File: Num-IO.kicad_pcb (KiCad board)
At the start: 4 copper layers, 170.2 x 77.5 mm, 143 parts, among them J1 DB37_Female, J2 DB37_Male, J3 Conn_02x25_Odd_Even, J4 0826-1X1T-GH-F, U1 MAX14917AFM+, U10 LTC6820IUD, U11 LTC6820IUD, U12 LTC6820IUD, U13 LTC6820IUD, U2 MAX14917AFM+, U3 74LVC1G18, U4 MAX14851AEE+, U5 MAX14917AFM+, U6 MAX31910AUI+, U7 MAX31910AUI+, U8 MAX31910AUI+, U9 MAX31910AUI+

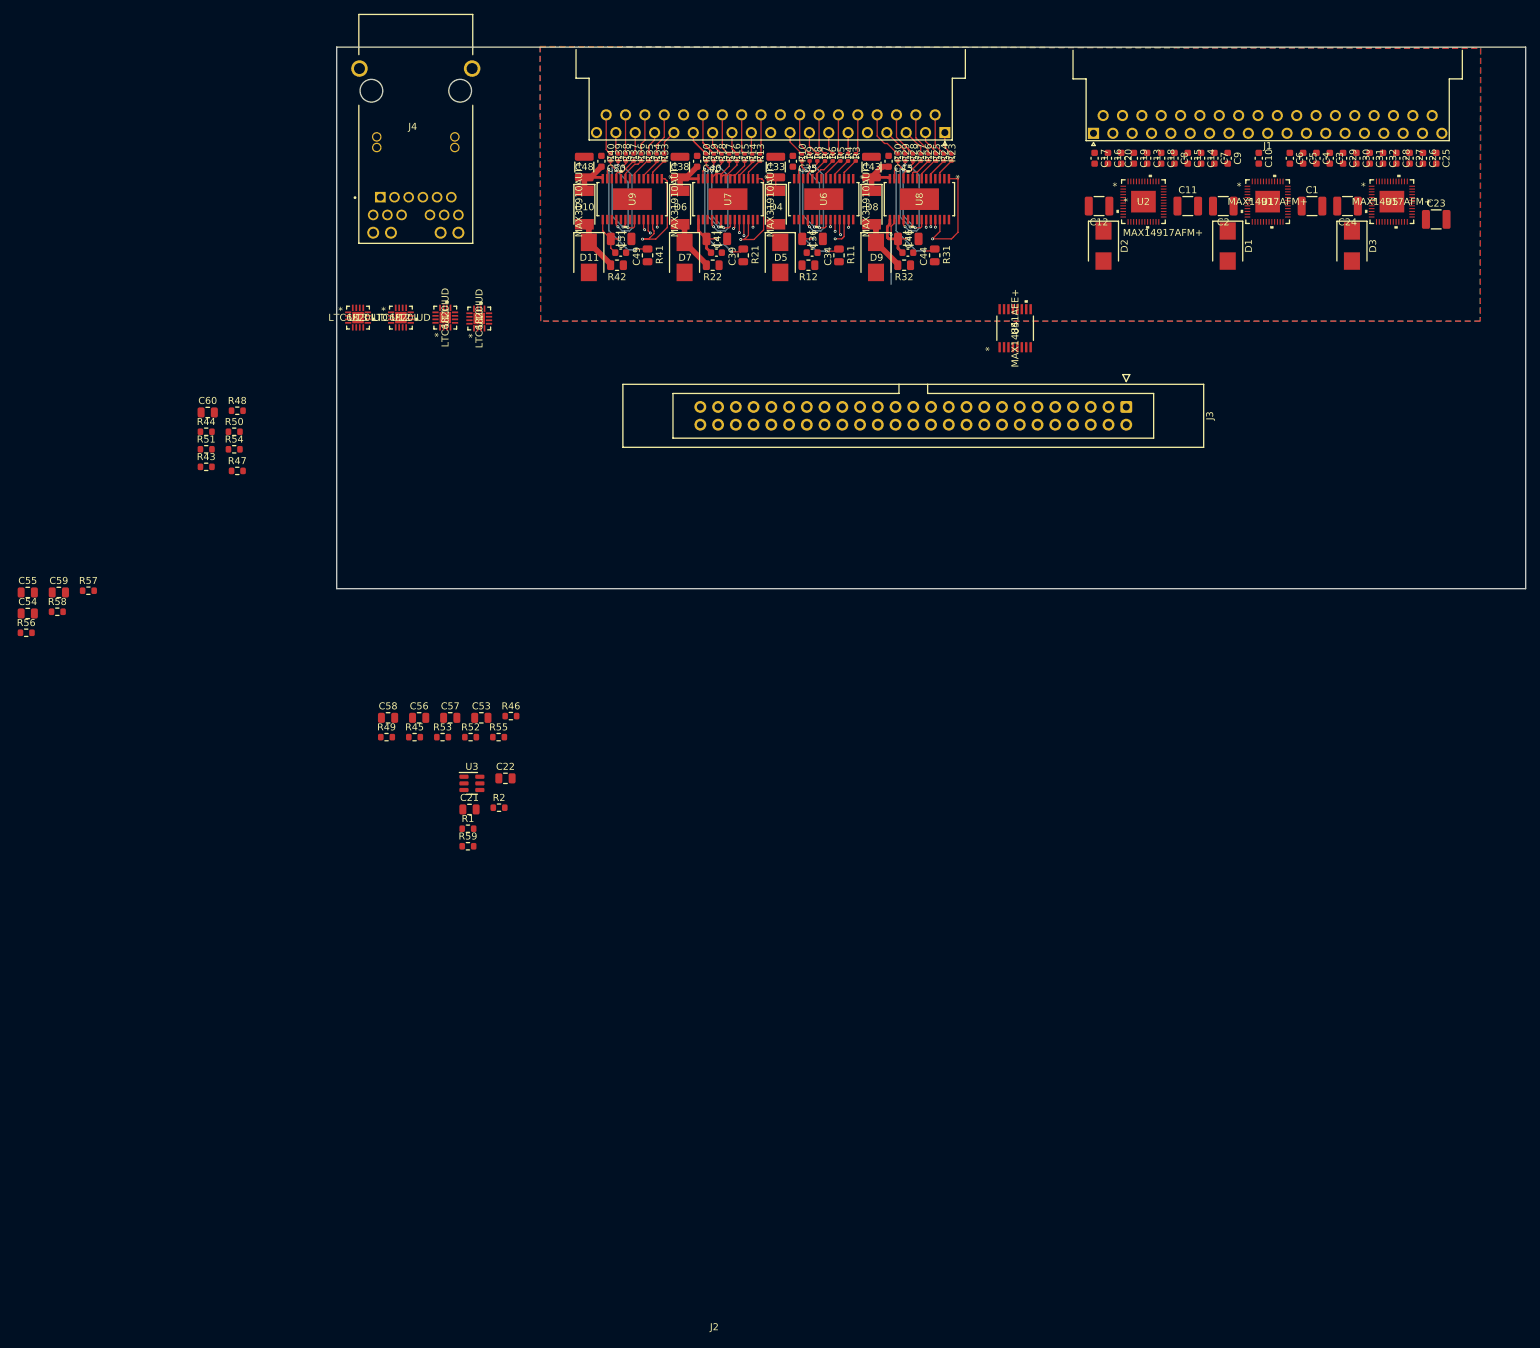
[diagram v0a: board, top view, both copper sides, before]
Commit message: Common power stage for field IO
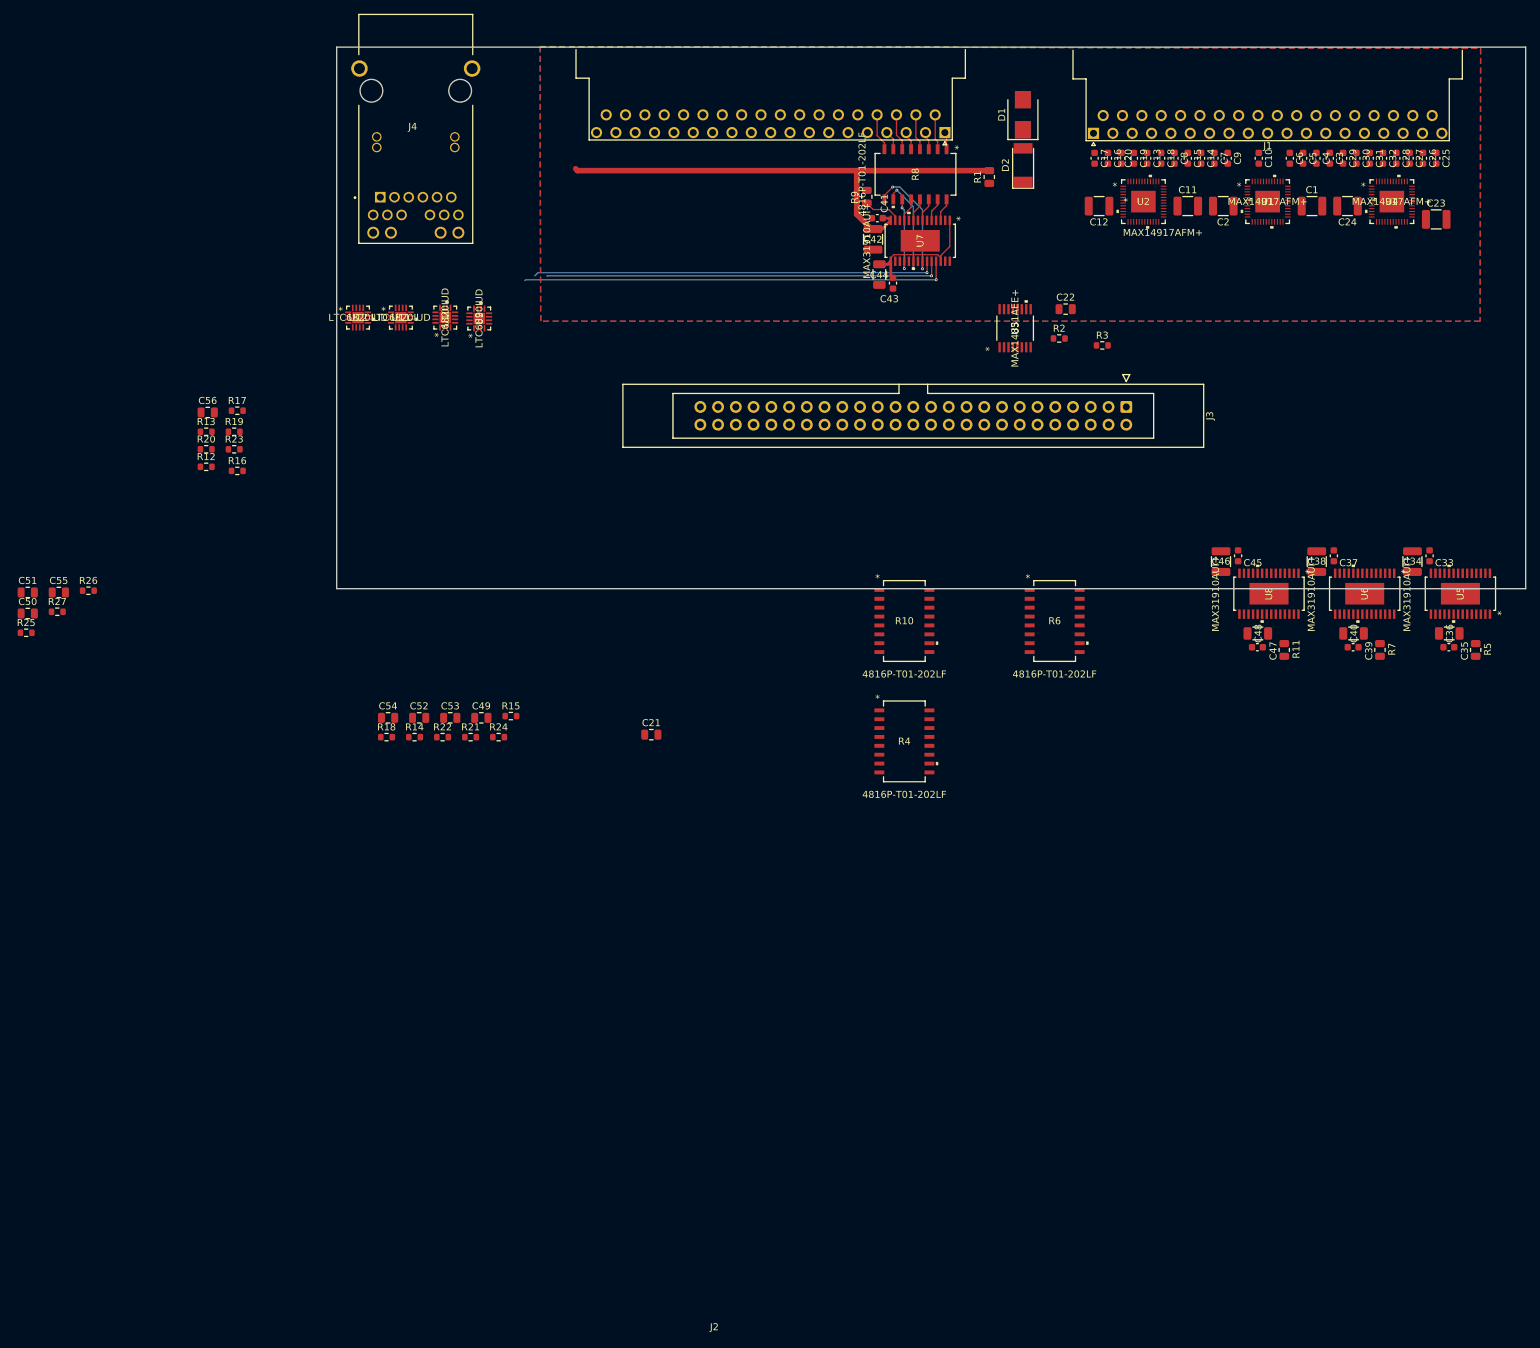
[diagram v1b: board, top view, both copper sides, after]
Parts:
- removed D10, D4, D6, D8: 1N4007, Diode_SMD:D_MELF
- removed D11, D5, D7, D9: SM6T36A, Diode_SMD:D_SMB
- removed D3: SM6F36A, Diode_SMD:D_SMB
- removed the R12 at (127.3, 55.5)
- removed the R13 at (120.4, 40.0)
- removed the R14 at (119.3, 40.0)
- removed the R15 at (118.2, 40.0)
- removed the R16 at (117.1, 40.0)
- removed the R17 at (116.0, 40.0)
- removed the R18 at (114.9, 40.0)
- removed the R19 at (113.8, 40.0)
- removed the R20 at (112.7, 40.0)
- removed the R22 at (113.6, 55.5)
- removed the R23 at (147.8, 40.0)
- removed the R24 at (146.7, 40.0)
- removed the R25 at (145.6, 40.0)
- removed the R26 at (144.5, 40.0)
- removed the R27 at (143.4, 40.0)
- removed R28, R29, R30, R33, R34, R35, R36, R37, R38, R39, R40: 2.2k, Resistor_SMD:R_0402_1005Metric
- removed the R3 at (134.1, 40.0)
- removed R32, R42: 150R, Resistor_SMD:R_0805_2012Metric
- removed the R5 at (131.9, 40.0)
- removed the R7 at (129.7, 40.0)
- removed the R9 at (127.5, 40.0)
- removed the U3 at (79.2, 129.6)
- D1: value SM6F36A -> SM6T36A
- D2: value SM6F36A -> 1N4007; footprint Diode_SMD:D_SMB -> Diode_SMD:D_MELF
- R1: value 3.3k -> 150R; footprint Resistor_SMD:R_0603_1608Metric -> Resistor_SMD:R_0805_2012Metric
- R10, R4, R6, R8: value 2.2k -> 4816P-T01-202LF; footprint Resistor_SMD:R_0402_1005Metric -> Maxim industrial IO:4816P
- moved R1 119.4 mm to (153.2, 42.8), turned to 90 degrees
- moved R3 115.7 mm to (169.4, 66.9)
- moved C34 107.2 mm to (213.8, 97.9)
- moved C37 107.2 mm to (202.5, 97.0)
- moved C47 107.2 mm to (191.6, 110.1)
- moved C33 107.2 mm to (216.2, 97.0)
- moved C35 107.2 mm to (219.0, 110.1)
- moved C36 107.2 mm to (219.0, 108.2)
- moved C38 107.2 mm to (200.1, 97.9)
- moved C39 107.2 mm to (205.3, 110.1)
- moved C40 107.2 mm to (205.3, 108.2)
- moved C45 107.2 mm to (188.8, 97.0)
- moved C46 107.2 mm to (186.4, 97.9)
- moved C48 107.2 mm to (191.6, 108.2)
- moved R11 107.2 mm to (195.4, 110.5)
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- renumbered C35 to C33, C33 to C34, C34 to C35, C40 to C37, C41 to C40, C45 to C41, C43 to C42, C44 to C43, C46 to C44, C50 to C45, C48 to C46, C49 to C47, C51 to C48, C53 to C49, C54 to C50, C55 to C51, C56 to C52, C57 to C53, C58 to C54, C59 to C55, C60 to C56, R41 to R11, R43 to R12, R44 to R13, R45 to R14, R46 to R15, R47 to R16, R48 to R17, R49 to R18, R50 to R19, R51 to R20, R52 to R21, R53 to R22, R54 to R23, R55 to R24, R56 to R25, R57 to R26, R58 to R27, R59 to R3, R11 to R5, R21 to R7, R31 to R9, U11 to U10, U12 to U11, U13 to U12, U4 to U3, U5 to U4, U6 to U5, U7 to U6, U8 to U7, U9 to U8, U10 to U9
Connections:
- net GND renamed GNDD
- C12 pad 1: +24V -> OUTPWR
- C2 pad 1: +24V -> OUTPWR
- C24 pad 1: +24V -> OUTPWR
- C33 pad 1: Net-(C33-Pad1) -> INPWR
- C34 pad 1: Net-(C33-Pad1) -> INPWR
- C37 pad 1: Net-(C38-Pad1) -> INPWR
- C38 pad 1: Net-(C38-Pad1) -> INPWR
- C41 pad 1: Net-(C43-Pad1) -> INPWR
- C42 pad 1: Net-(C43-Pad1) -> INPWR
- C45 pad 1: Net-(C48-Pad1) -> INPWR
- C46 pad 1: Net-(C48-Pad1) -> INPWR
- D2 pad 1: +24V -> OUTPWR
- D2 pad 2: GNDPWR -> +24V
- R1 pad 1: /CS0 -> OUTPWR
- R1 pad 2: /IsoPWR -> INPWR
- R10 pad 1: /Input connector/IN16 -> /Input connector/IN25
- R10 pad 2: Net-(R10-Pad2) -> /Input connector/IN26
- R2 pad 1: /CS1 -> /CS
- R4 pad 1: /Input connector/IN10 -> /Input connector/IN9
- R4 pad 2: Net-(R4-Pad2) -> /Input connector/IN10
- R6 pad 1: /Input connector/IN12 -> /Input connector/IN17
- R6 pad 2: Net-(R6-Pad2) -> /Input connector/IN18
- R8 pad 1: /Input connector/IN14 -> /Input connector/IN1
- R8 pad 2: Net-(R8-Pad2) -> /Input connector/IN2
- U1 pad 30: /CS1 -> /CS
- U1 pad 49: +24V -> OUTPWR
- U1 pad 8: +24V -> OUTPWR
- U2 pad 30: /CS1 -> /CS
- U2 pad 34: /SDO -> GNDPWR
- U2 pad 49: +24V -> OUTPWR
- U2 pad 8: +24V -> OUTPWR
- U3 pad 10: /CS0 -> unconnected-(U3-Pad10)
- U3 pad 11: /CS1 -> /CS
- U3 pad 6: Net-(U3-Pad6) -> /FPGA Connector/SPI0.*CS
- U3 pad 7: Net-(U3-Pad4) -> unconnected-(U3-Pad7)
- U4 pad 30: /CS1 -> /CS
- U4 pad 49: +24V -> OUTPWR
- U4 pad 8: +24V -> OUTPWR
- U5 pad 11: Net-(R7-Pad2) (its old number) -> Net-(R4-Pad12)
- U5 pad 14: Net-(C33-Pad1) -> INPWR
- U5 pad 18: Net-(R8-Pad2) -> Net-(R4-Pad11)
- U5 pad 20: Net-(R9-Pad2) (its old number) -> Net-(R4-Pad10)
- U5 pad 22: Net-(R10-Pad2) -> Net-(R4-Pad9)
- U5 pad 24: /CS0 -> /CS
- U5 pad 3: Net-(R3-Pad2) -> Net-(R4-Pad16)
- U5 pad 5: Net-(R4-Pad2) -> Net-(R4-Pad15)
- U5 pad 7: Net-(R5-Pad2) (its old number) -> Net-(R4-Pad14)
- U5 pad 9: Net-(R6-Pad2) -> Net-(R4-Pad13)
- U6 pad 11: Net-(R17-Pad2) (its old number) -> Net-(R6-Pad12)
- U6 pad 14: Net-(C38-Pad1) -> INPWR
- U6 pad 18: Net-(R18-Pad2) (its old number) -> Net-(R6-Pad11)
- U6 pad 20: Net-(R19-Pad2) (its old number) -> Net-(R6-Pad10)
- U6 pad 22: Net-(R20-Pad2) -> Net-(R6-Pad9)
- U6 pad 24: /CS0 -> /CS
- U6 pad 3: Net-(R13-Pad2) -> Net-(R6-Pad16)
- U6 pad 5: Net-(R14-Pad2) -> Net-(R6-Pad15)
- U6 pad 7: Net-(R15-Pad2) -> Net-(R6-Pad14)
- U6 pad 9: Net-(R16-Pad2) (its old number) -> Net-(R6-Pad13)
- U7 pad 11: Net-(R27-Pad2) -> Net-(R8-Pad12)
- U7 pad 14: Net-(C43-Pad1) -> INPWR
- U7 pad 18: Net-(R28-Pad2) -> Net-(R8-Pad11)
- U7 pad 20: Net-(R29-Pad2) -> Net-(R8-Pad10)
- U7 pad 22: Net-(R30-Pad2) -> Net-(R8-Pad9)
- U7 pad 24: /CS0 -> /CS
- U7 pad 3: Net-(R23-Pad2) -> Net-(R8-Pad16)
- U7 pad 5: Net-(R24-Pad2) -> Net-(R8-Pad15)
- U7 pad 7: Net-(R25-Pad2) -> Net-(R8-Pad14)
- U7 pad 9: Net-(R26-Pad2) -> Net-(R8-Pad13)
- U8 pad 11: Net-(R37-Pad2) -> Net-(R10-Pad12)
- U8 pad 14: Net-(C48-Pad1) -> INPWR
- U8 pad 18: Net-(R38-Pad2) -> Net-(R10-Pad11)
- U8 pad 20: Net-(R39-Pad2) -> Net-(R10-Pad10)
- U8 pad 22: Net-(R40-Pad2) -> Net-(R10-Pad9)
- U8 pad 24: /CS0 -> /CS
- U8 pad 3: Net-(R33-Pad2) -> Net-(R10-Pad16)
- U8 pad 5: Net-(R34-Pad2) -> Net-(R10-Pad15)
- U8 pad 7: Net-(R35-Pad2) -> Net-(R10-Pad14)
- U8 pad 9: Net-(R36-Pad2) -> Net-(R10-Pad13)
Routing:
- net INPWR: track 0.00 -> 73.1 mm
- net /CS: track 0.00 -> 57.1 mm, vias 0 -> 1
- net /CS0: track 48.1 -> 0.00 mm, vias 4 -> 0
- net /input channel 1-8/SDO: track 13.8 -> 58.0 mm, vias 2 -> 1
- net /IsoPWR: track 26.1 -> 0.00 mm, vias 2 -> 0
- net /input channel 17-24/5VOUT: track 25.9 -> 0.00 mm, vias 2 -> 0
- net Net-(R7-Pad2): track 17.6 -> 0.00 mm, vias 2 -> 0
- net Net-(R8-Pad9): track 0.00 -> 17.4 mm, vias 0 -> 2
- net Net-(R5-Pad2): track 17.3 -> 0.00 mm, vias 2 -> 0
- net Net-(R11-Pad2): track 17.0 -> 0.00 mm, vias 2 -> 0
- net Net-(R8-Pad10): track 0.00 -> 14.8 mm, vias 0 -> 2
- net Net-(R18-Pad2) (its old number): track 13.9 -> 0.00 mm, vias 2 -> 0
- net Net-(R38-Pad2): track 13.9 -> 0.00 mm, vias 2 -> 0
- net Net-(R8-Pad2): track 13.9 -> 0.00 mm, vias 2 -> 0
- net Net-(R28-Pad2): track 13.9 -> 0.00 mm, vias 2 -> 0
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
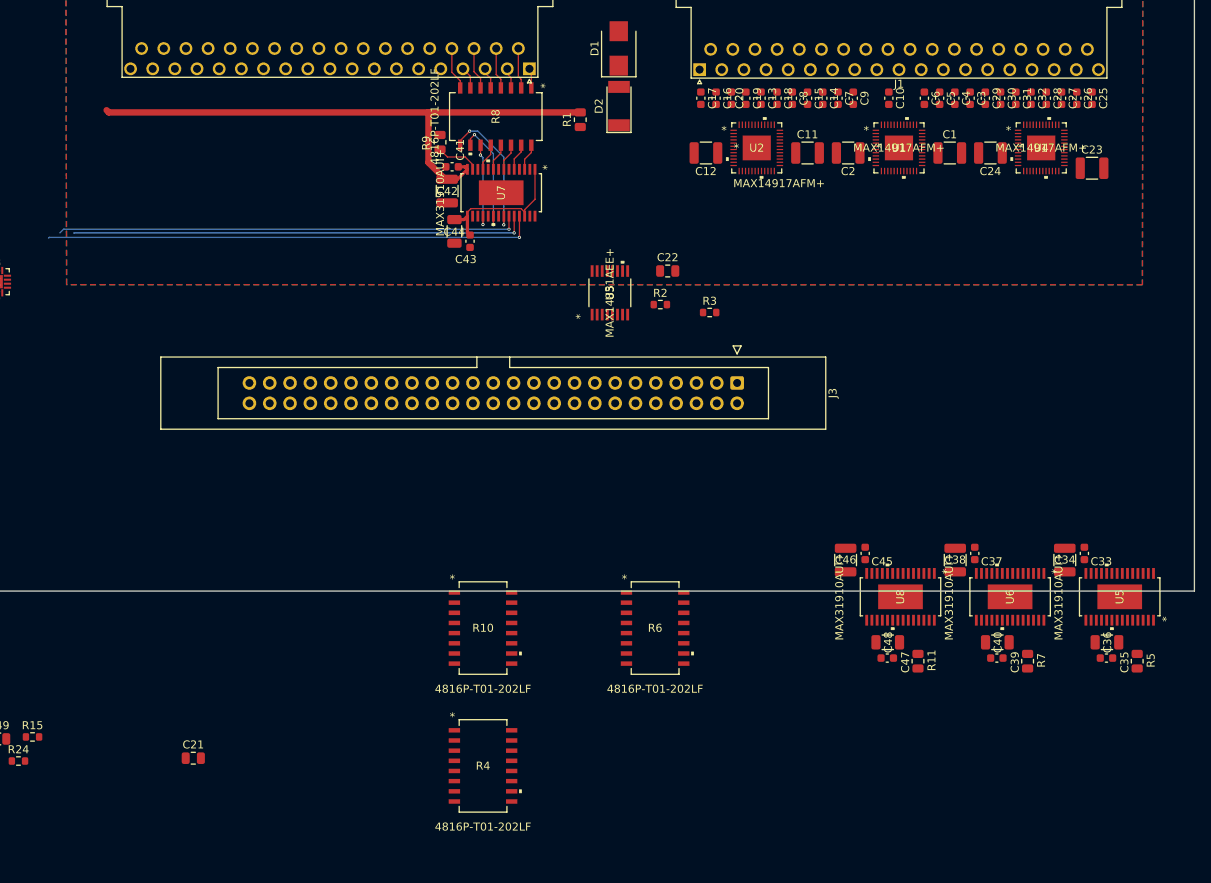
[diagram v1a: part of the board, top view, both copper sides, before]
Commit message: Further simplifying the schematics
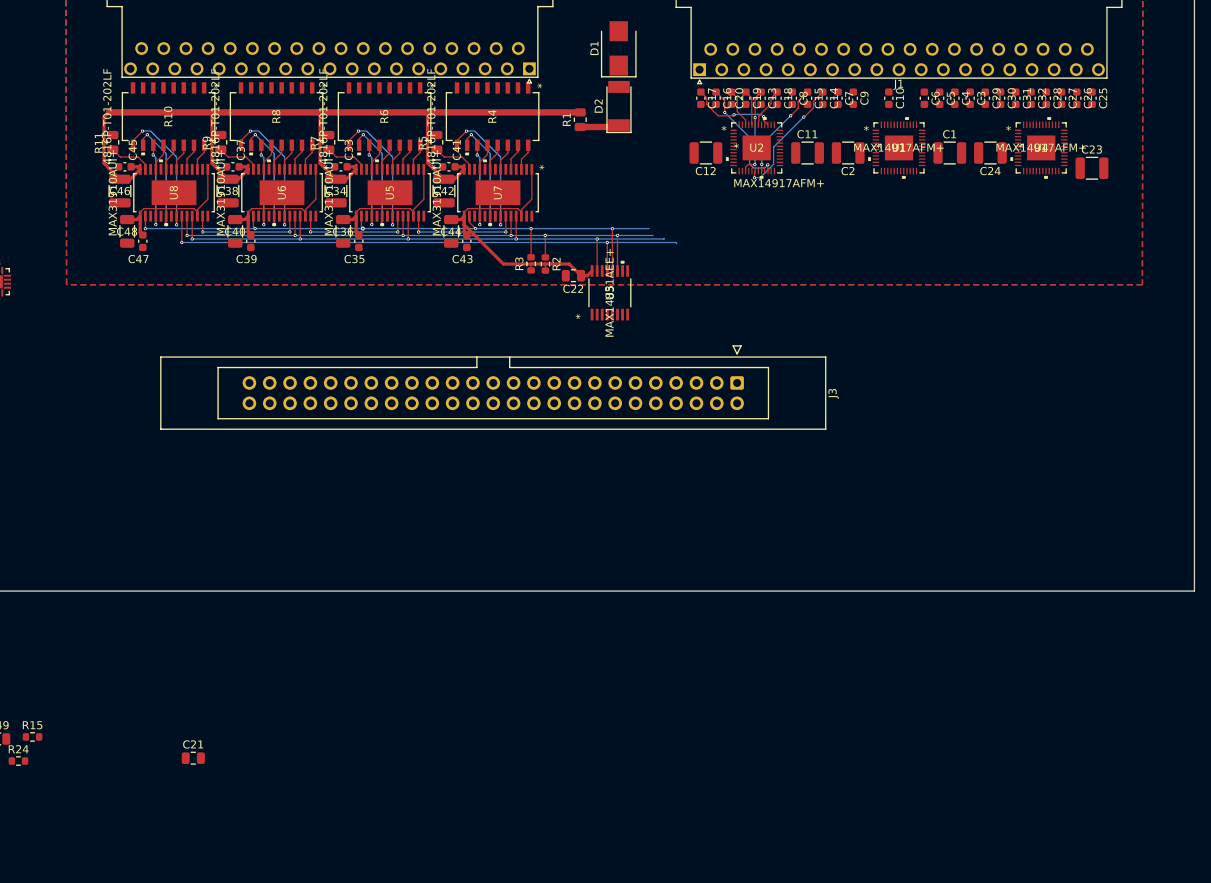
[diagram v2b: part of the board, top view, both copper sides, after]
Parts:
- moved R7 120.1 mm to (121.8, 45.6), turned to -90 degrees
- moved R9 119.9 mm to (108.3, 45.6), turned to -90 degrees
- moved R11 119.7 mm to (94.8, 45.6), turned to -90 degrees
- moved C36 108.4 mm to (123.6, 56.8), turned to -90 degrees
- moved C40 108.2 mm to (110.1, 56.8), turned to -90 degrees
- moved C48 108.1 mm to (96.6, 56.8), turned to -90 degrees
- moved C35 107.0 mm to (125.5, 58.0), turned to -90 degrees
- moved C39 106.8 mm to (112.0, 58.0), turned to -90 degrees
- moved C47 106.6 mm to (98.5, 58.0), turned to -90 degrees
- moved C33 104.7 mm to (123.3, 48.7), turned to 180 degrees
- moved C37 104.6 mm to (109.8, 48.7), turned to 180 degrees
- moved C45 104.4 mm to (96.3, 48.7), turned to 180 degrees
- moved U5 104.3 mm to (129.4, 52.0)
- moved U6 104.1 mm to (115.9, 52.0)
- moved U8 103.9 mm to (102.4, 52.0)
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- renumbered R8 to R4, R9 to R5, R4 to R6, R5 to R7, R6 to R8, R7 to R9
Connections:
- C43 pad 1: /input channel 1-8/5VOUT -> /IsoPWR
- C44 pad 1: /input channel 1-8/5VOUT -> /IsoPWR
- C47 pad 1: /IsoPWR -> /input channel 25-32/5VOUT
- C48 pad 1: /IsoPWR -> /input channel 25-32/5VOUT
- R3 pad 1: /output channel 1-8/VL -> /IsoPWR
- U7 pad 1: /input channel 1-8/5VOUT -> /IsoPWR
- U7 pad 15: /input channel 1-8/5VOUT -> /IsoPWR
- U7 pad 26: /input channel 1-8/5VOUT -> /IsoPWR
- U8 pad 1: /IsoPWR -> /input channel 25-32/5VOUT
- U8 pad 15: /IsoPWR -> /input channel 25-32/5VOUT
- U8 pad 26: /IsoPWR -> /input channel 25-32/5VOUT
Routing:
- net /*FAULT: track 0.00 -> 78.5 mm, vias 0 -> 6
- net /SDO: track 0.00 -> 68.8 mm, vias 0 -> 2
- net /input channel 1-8/SDO: track 58.0 -> 14.9 mm, vias 1 -> 2
- net INPWR: track 73.1 -> 114.4 mm
- net /IsoPWR: track 0.00 -> 40.9 mm
- net /input channel 9-16/5VOUT: track 0.00 -> 19.2 mm
- net /input channel 25-32/5VOUT: track 0.00 -> 19.2 mm
- net /input channel 17-24/5VOUT: track 0.00 -> 19.2 mm
- net /input channel 1-8/5VOUT: track 19.2 -> 0.00 mm
- net /CS: track 57.1 -> 75.2 mm, vias 1 -> 6
- net Net-(R8-Pad9): track 0.00 -> 17.4 mm, vias 0 -> 2
- net Net-(R6-Pad9): track 0.00 -> 17.4 mm, vias 0 -> 2
- net Net-(R10-Pad9): track 0.00 -> 17.4 mm, vias 0 -> 2
- net /output channel 17-24/OUT2: track 0.00 -> 15.6 mm, vias 0 -> 2
- net Net-(R8-Pad10): track 0.00 -> 14.8 mm, vias 0 -> 2
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- removed copper zone on In1.Cu, net GNDPWR
- removed copper zone on In2.Cu, net GNDPWR
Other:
- copper layers 4 -> 2

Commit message: fix DRC errors
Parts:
- moved C51 193.7 mm to (209.3, 99.2), turned to -90 degrees
- moved C55 191.6 mm to (211.6, 99.2), turned to -90 degrees
- moved R26 189.7 mm to (213.8, 96.7), turned to -90 degrees
- moved C52 146.5 mm to (211.8, 77.6)
- moved R18 145.7 mm to (209.1, 91.2), turned to 180 degrees
- moved U11 145.3 mm to (210.7, 95.2)
- moved C53 143.6 mm to (211.6, 72.9)
- moved C49 141.2 mm to (216.1, 81.0)
- moved C54 141.2 mm to (202.8, 81.0)
- moved R15 141.2 mm to (220.3, 80.8)
- moved R21 141.2 mm to (214.6, 83.8)
- moved R24 141.2 mm to (218.6, 83.8)
- moved R22 140.3 mm to (211.4, 90.5), turned to -90 degrees
- moved R14 139.5 mm to (207.4, 93.7), turned to -90 degrees
- moved C21 131.5 mm to (226.3, 72.3)
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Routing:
- net GNDPWR: track 0.00 -> 9.33 mm
- net Net-(R11-Pad2): track 5.46 -> 0.00 mm
- net /CLK: track 74.5 -> 76.2 mm
- net /CS: track 75.2 -> 76.3 mm
- net Net-(R10-Pad9): track 17.4 -> 18.2 mm
- net Net-(R10-Pad10): track 14.8 -> 15.5 mm
- net /input channel 1-8/SDO: track 14.9 -> 15.5 mm
- net /input channel 17-24/5VOUT: track 19.2 -> 18.6 mm
- net Net-(R10-Pad11): track 11.1 -> 11.7 mm
